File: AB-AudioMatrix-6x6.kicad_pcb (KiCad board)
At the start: 4 copper layers, 200 x 70 mm, 75 parts, among them J1 Switchcraft-35RAPC4BH3, J10 Switchcraft-35RAPC4BH3, J11 Switchcraft-35RAPC4BH3, J12 Switchcraft-35RAPC4BH3, J13 Conn_01x24, J14 Conn_01x24, J15 Screw_Terminal_01x03, J16 Conn_01x24, J17 Conn_01x24, J2 Switchcraft-35RAPC4BH3, J3 Switchcraft-35RAPC4BH3, J4 Switchcraft-35RAPC4BH3, J5 Switchcraft-35RAPC4BH3, J6 Switchcraft-35RAPC4BH3, J7 Switchcraft-35RAPC4BH3, J8 Switchcraft-35RAPC4BH3, J9 Switchcraft-35RAPC4BH3, SW1 SW_Rotary2x6, SW2 SW_Rotary2x6, SW3 SW_Rotary2x6, SW4 SW_Rotary2x6, SW5 SW_Rotary2x6, SW6 SW_Rotary2x6, U1 TL072, U2 TL072, U3 TL072, U4 TL072, U5 TL072, U6 TL072, U7 TL072

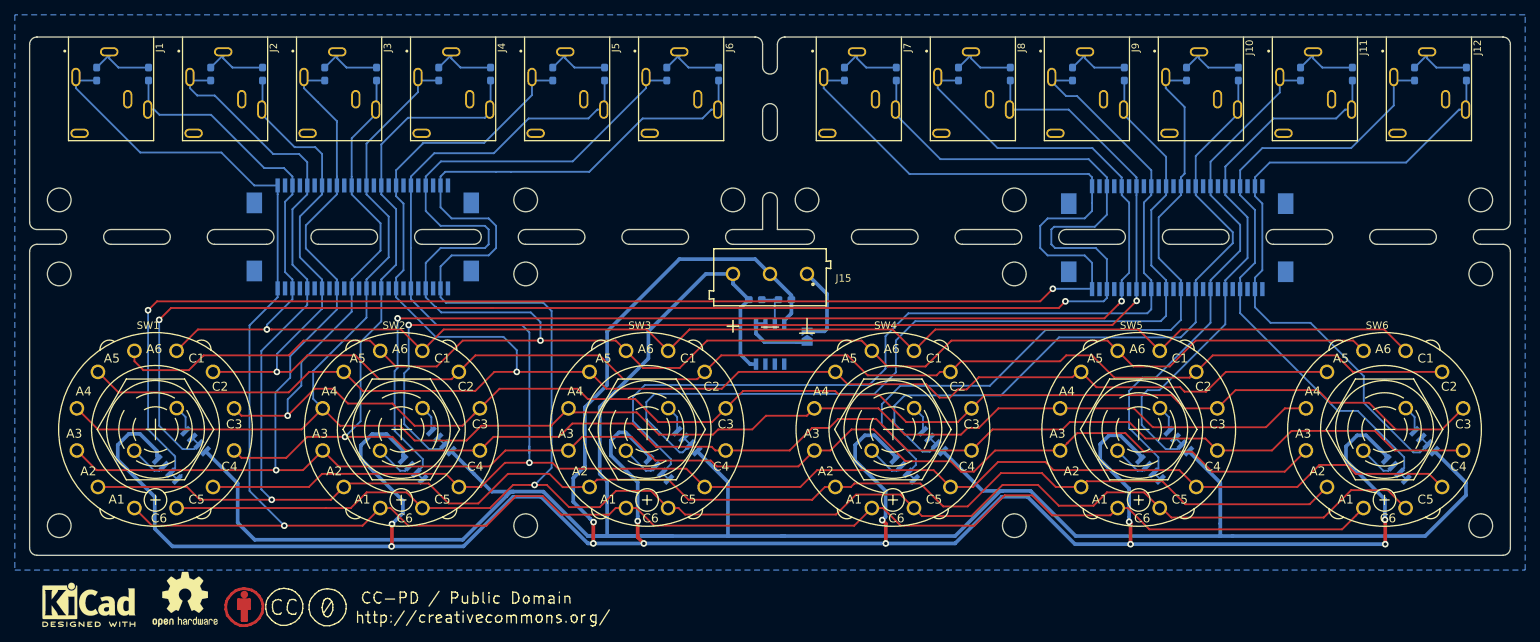
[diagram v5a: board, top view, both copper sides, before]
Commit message: finished routing | added GND polygon | added description in surface plot  | added pictures to README.md documentation | changed LICENCE.md to CC BY 4.0
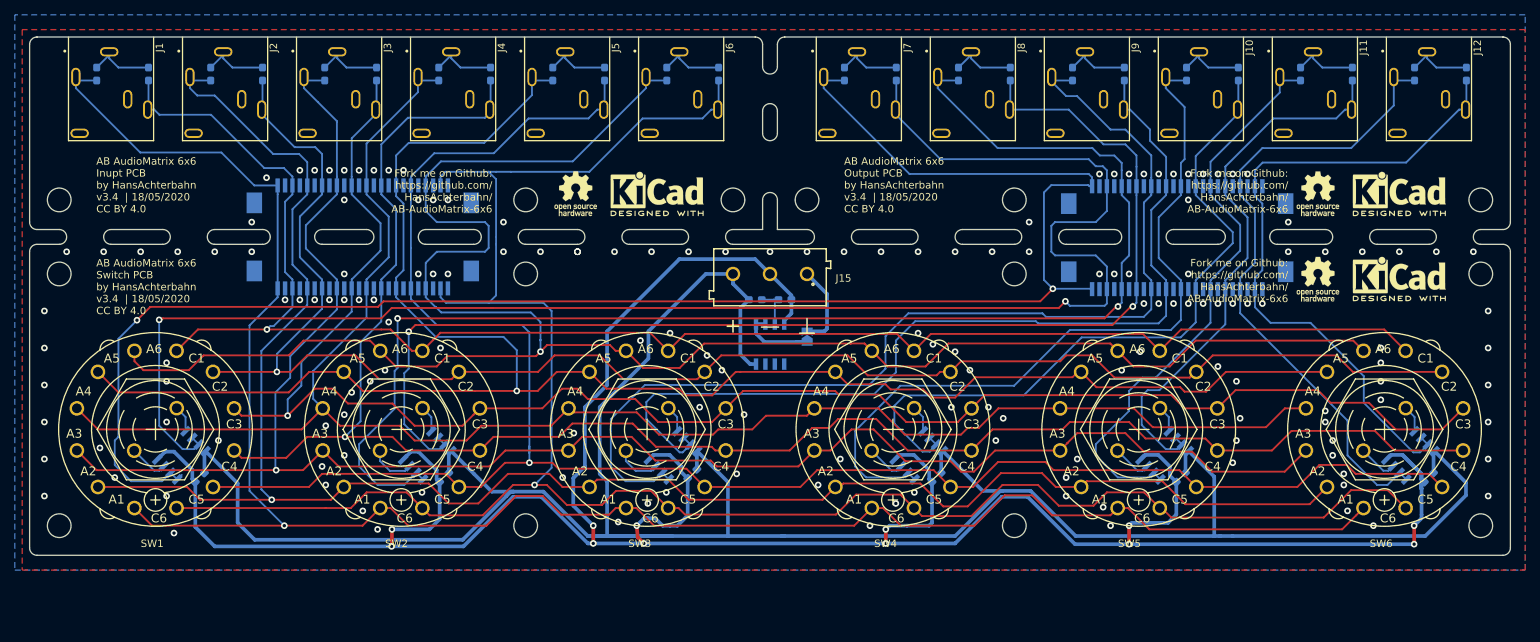
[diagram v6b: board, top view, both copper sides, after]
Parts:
- removed ?: Symbol_CreativeCommonsPublicDomain_SilkScreenTop_Small, Symbol:Symbol_CreativeCommonsPublicDomain_SilkScreenTop_Small
- removed the REF** at (51.0, 154.7)
- removed the REF** at (64.0, 154.0)
- removed the REF** at (72.0, 155.0)
- added C1: 100n, Capacitor_SMD:C_0603_1608Metric_Pad1.05x0.95mm_HandSolder, B.Cu at (66.0, 137.5)
- added C2: 100n, Capacitor_SMD:C_0603_1608Metric_Pad1.05x0.95mm_HandSolder, B.Cu at (99.0, 137.5)
- added C3: 100n, Capacitor_SMD:C_0603_1608Metric_Pad1.05x0.95mm_HandSolder, B.Cu at (132.5, 137.0)
- added C4: 100n, Capacitor_SMD:C_0603_1608Metric_Pad1.05x0.95mm_HandSolder, B.Cu at (165.5, 137.5)
- added C5: 100n, Capacitor_SMD:C_0603_1608Metric_Pad1.05x0.95mm_HandSolder, B.Cu at (198.5, 137.5)
- added C6: 100n, Capacitor_SMD:C_0603_1608Metric_Pad1.05x0.95mm_HandSolder, B.Cu at (232.0, 137.5)
- added REF**: KiCad-Logo2_6mm_SilkScreen, Symbol:KiCad-Logo2_6mm_SilkScreen, F.Cu at (127.8, 99.2)
- added REF**: OSHW-Logo_5.7x6mm_SilkScreen, Symbol:OSHW-Logo_5.7x6mm_SilkScreen, F.Cu at (116.8, 99.2)
- added REF**: KiCad-Logo2_6mm_SilkScreen, Symbol:KiCad-Logo2_6mm_SilkScreen, F.Cu at (228.0, 110.7)
- added REF**: KiCad-Logo2_6mm_SilkScreen, Symbol:KiCad-Logo2_6mm_SilkScreen, F.Cu at (228.0, 99.2)
- added REF**: OSHW-Logo_5.7x6mm_SilkScreen, Symbol:OSHW-Logo_5.7x6mm_SilkScreen, F.Cu at (217.0, 99.2)
- added REF**: OSHW-Logo_5.7x6mm_SilkScreen, Symbol:OSHW-Logo_5.7x6mm_SilkScreen, F.Cu at (217.0, 110.7)
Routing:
- net +9V: track 317.8 -> 335.2 mm
- net -9V: track 383.3 -> 368.0 mm
- net Out2L: track 174.9 -> 185.1 mm
- net Out3L: track 133.2 -> 140.8 mm
- net Out5L: track 72.4 -> 79.4 mm
- net In6R: track 296.2 -> 289.3 mm
- net Out4L: track 97.6 -> 103.9 mm
- net In5L: track 245.6 -> 250.1 mm
- net Out1L: track 227.6 -> 230.5 mm
- net Out6L: track 86.0 -> 88.0 mm
- net Out1R: track 217.7 -> 219.1 mm
- net Out2R: track 163.6 -> 164.9 mm
- net In1R: track 228.1 -> 227.0 mm
- net In6L: track 270.9 -> 271.9 mm
- net Net-(SW3-Pad13): track 5.39 -> 6.23 mm
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- added copper zone on F.Cu, net GND
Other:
- outline, holes or cut-outs redrawn
- board text added: "AB AudioMatrix 6x6 Inupt PCB by HansAchterbahn v3.4 | 18/05/2020 CC BY 4.0"
- board text added: "AB AudioMatrix 6x6 Output PCB by HansAchterbahn v3.4 | 18/05/2020 CC BY 4.0"
- board text added: "AB AudioMatrix 6x6 Switch PCB by HansAchterbahn v3.4 | 18/05/2020 CC BY 4.0"
- board text added: "Fork me on Github: https://github.com/ HansAchterbahn/ AB-AudioMatrix-6x6"
